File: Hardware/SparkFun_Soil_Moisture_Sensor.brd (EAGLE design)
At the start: 22.9 x 61 mm, 23 parts, among them J1 GATORGATOR_MINI, J2 GATORGATOR_MINI, J3 GATORGATOR_MINI, Q1 2N3904

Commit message: updating silk, fiducials
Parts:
- moved FID1 5.21 mm to (21.6, 56.1)
- moved FID4 5.21 mm to (21.6, 56.1)
- moved U$4 1.27 mm to (14.7, 55.0)
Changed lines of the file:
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@@
 <element name="LOGO1" library="SparkFun-Aesthetics" package="SFE_LOGO_NAME_FLAME_.1" value="SFE_LOGO_NAME_FLAME.1_INCH" x="17.399" y="45.847" smashed="yes" rot="MR0"/>
 <element name="LOGO2" library="SparkFun-Aesthetics" package="OSHW-LOGO-S" value="OSHW-LOGOS" x="20.32" y="54.61" smashed="yes" rot="MR0"/>
-<element name="U$4" library="SparkFun-Aesthetics" package="SFE_LOGO_FLAME_.2" value="" x="14.732" y="53.721" smashed="yes"/>
+<element name="U$4" library="SparkFun-Aesthetics" package="SFE_LOGO_FLAME_.2" value="" x="14.732" y="54.991" smashed="yes"/>
 <element name="STANDOFF1" library="SparkFun-Electromechanical" package="STAND-OFF" value="STAND-OFF" x="2.54" y="58.42" smashed="yes"/>
 <element name="STANDOFF2" library="SparkFun-Electromechanical" package="STAND-OFF" value="STAND-OFF" x="20.32" y="58.42" smashed="yes"/>
-<element name="FID1" library="SparkFun-Aesthetics" package="FIDUCIAL-1X2" value="FIDUCIAL1X2" x="17.78" y="59.69" smashed="yes"/>
+<element name="FID1" library="SparkFun-Aesthetics" package="FIDUCIAL-1X2" value="FIDUCIAL1X2" x="21.59" y="56.134" smashed="yes"/>
 <element name="FID2" library="SparkFun-Aesthetics" package="FIDUCIAL-1X2" value="FIDUCIAL1X2" x="1.27" y="45.72" smashed="yes"/>
 <element name="J1" library="SparkFun-Connectors" package="GATOR_MINI" value="GATORGATOR_MINI" x="3.81" y="52.07" smashed="yes" rot="R270"/>
@@
 <element name="J3" library="SparkFun-Connectors" package="GATOR_MINI" value="GATORGATOR_MINI" x="11.43" y="57.15" smashed="yes" rot="R180"/>
 <element name="FID3" library="SparkFun-Aesthetics" package="FIDUCIAL-1X2" value="FIDUCIAL1X2" x="1.27" y="45.72" smashed="yes" rot="MR0"/>
-<element name="FID4" library="SparkFun-Aesthetics" package="FIDUCIAL-1X2" value="FIDUCIAL1X2" x="17.78" y="59.69" smashed="yes" rot="MR0"/>
+<element name="FID4" library="SparkFun-Aesthetics" package="FIDUCIAL-1X2" value="FIDUCIAL1X2" x="21.59" y="56.134" smashed="yes" rot="MR0"/>
 <element name="U$1" library="buzzard_labels (2)" package="PWR2" value="" x="7.747" y="49.53" smashed="yes" rot="R90"/>
 <element name="U$2" library="buzzard_labels (2)" package="GND0" value="" x="15.24" y="54.483" smashed="yes" rot="R270"/>

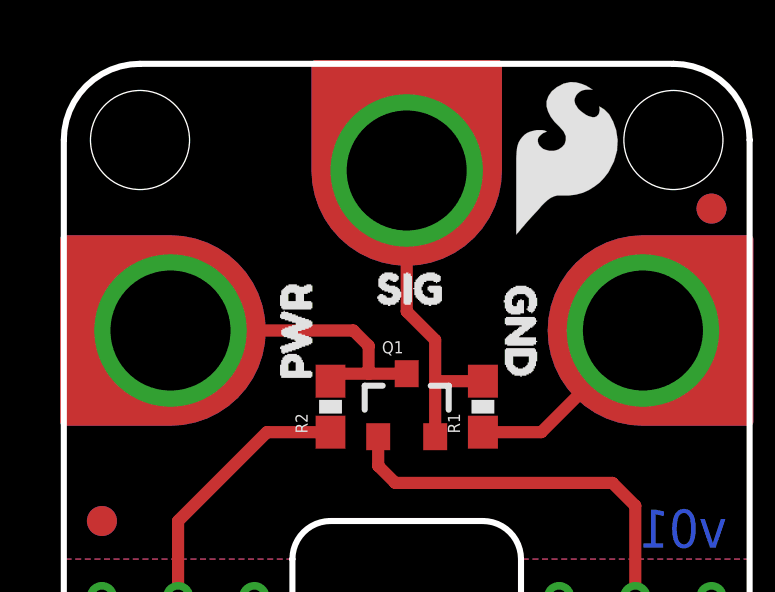
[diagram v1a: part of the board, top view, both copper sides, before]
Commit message: adding protection circuitry
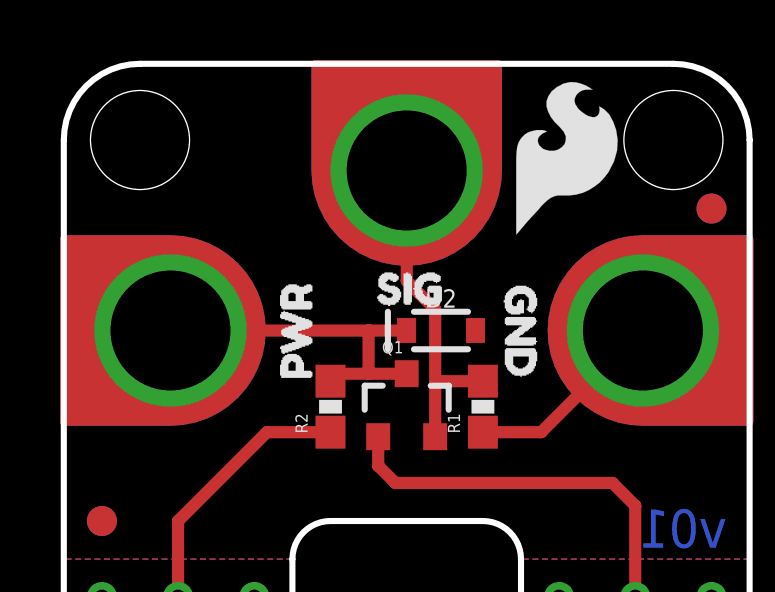
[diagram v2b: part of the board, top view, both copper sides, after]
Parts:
- added D2: 3.6V, SparkFun-DiscreteSemi:SOD-323
- Q1: device SparkFun-DiscreteSemi:SOT23-3 -> SparkFun-DiscreteSemi:SOT23-3@1
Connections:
- net GND: now also D2.A
- net VCC: now also D2.C
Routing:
- net VCC: track 10.4 -> 12.0 mm
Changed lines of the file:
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@@
 </autorouter>
 <elements>
-<element name="Q1" library="SparkFun-DiscreteSemi" package="SOT23-3" value="2N3904" x="11.43" y="49.53" smashed="yes">
+<element name="Q1" library="SparkFun-DiscreteSemi" package="SOT23-3@1" value="2N3904" x="11.43" y="49.53" smashed="yes">
 <attribute name="NAME" x="10.6045" y="51.308" size="0.4064" layer="25"/>
 <attribute name="PROD_ID" value="TRANS-08049" x="11.43" y="49.53" size="1.778" layer="27" font="vector" ratio="15" display="off"/>
@@
 <element name="U$7" library="buzzard_labels (2)" package="GND0" value="" x="15.24" y="49.657" smashed="yes" rot="MR90"/>
 <element name="LOGO3" library="SparkFun-Aesthetics" package="REVISION" value="REVISION" x="3.81" y="-12.7" smashed="yes"/>
+<element name="D2" library="SparkFun-DiscreteSemi" package="SOD-323" value="3.6V" x="12.573" y="52.07" smashed="yes">
+<attribute name="NAME" x="12.573" y="52.832" size="0.6096" layer="25" font="vector" ratio="20" align="bottom-center"/>
+<attribute name="PROD_ID" value="DIO-08199" x="12.573" y="52.07" size="1.778" layer="27" display="off"/>
+<attribute name="VALUE" x="12.573" y="51.308" size="0.6096" layer="27" font="vector" ratio="20" align="top-center"/>
+</element>
 </elements>
 <signals>
@@
 <contactref element="R1" pad="2"/>
 <contactref element="J3" pad="P$2"/>
-<wire x1="11.43" y1="57.404" x2="11.43" y2="52.705" width="0.4064" layer="1"/>
-<wire x1="11.43" y1="52.705" x2="12.38" y2="51.755" width="0.4064" layer="1"/>
-<wire x1="12.38" y1="51.755" x2="12.38" y2="50.292" width="0.4064" layer="1"/>
+<wire x1="11.43" y1="57.404" x2="11.43" y2="53.721" width="0.4064" layer="1"/>
+<wire x1="11.43" y1="53.721" x2="12.38" y2="52.771" width="0.4064" layer="1"/>
+<wire x1="12.38" y1="52.771" x2="12.38" y2="50.292" width="0.4064" layer="1"/>
 <wire x1="12.38" y1="50.292" x2="12.38" y2="48.53" width="0.4064" layer="1"/>
 <wire x1="12.468" y1="50.38" x2="12.38" y2="50.292" width="0.4064" layer="1"/>
@@
 <contactref element="J1" pad="P$2"/>
 <wire x1="10.16" y1="50.63" x2="11.43" y2="50.63" width="0.4064" layer="1"/>
-<wire x1="3.556" y1="52.07" x2="9.652" y2="52.07" width="0.4064" layer="1"/>
-<wire x1="9.652" y1="52.07" x2="10.16" y2="51.562" width="0.4064" layer="1"/>
-<wire x1="10.16" y1="51.562" x2="10.16" y2="50.63" width="0.4064" layer="1"/>
+<contactref element="D2" pad="C"/>
+<wire x1="3.556" y1="52.07" x2="10.16" y2="52.07" width="0.4064" layer="1"/>
+<wire x1="10.16" y1="52.07" x2="11.423" y2="52.07" width="0.4064" layer="1"/>
+<wire x1="10.16" y1="50.63" x2="10.16" y2="52.07" width="0.4064" layer="1"/>
 </signal>
 <signal name="GND">
@@
 <wire x1="19.304" y1="52.07" x2="15.914" y2="48.68" width="0.4064" layer="1"/>
 <wire x1="15.914" y1="48.68" x2="13.97" y2="48.68" width="0.4064" layer="1"/>
+<contactref element="D2" pad="A"/>
+<wire x1="13.723" y1="52.07" x2="13.97" y2="48.68" width="0" layer="19" extent="1-1"/>
 </signal>
 <signal name="PROBE1">

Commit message: finalizing silk and schematic before design review
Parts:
- added U$8: (no value), buzzard_labels (4):GATOR#SOIL_MOISTURE_SENSOR4
- added U$9: (no value), GatorBit_Final_for_Silk#01#png (2):GATORBIT_FINAL_FOR_SILK#01#PNG
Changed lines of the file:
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@@
 <?xml version="1.0" encoding="utf-8"?>
 <!DOCTYPE eagle SYSTEM "eagle.dtd">
-<eagle version="9.3.1">
+<eagle version="9.1.0">
 <drawing>
 <settings>
@@
 <attribute name="VALUE" x="12.573" y="51.308" size="0.6096" layer="27" font="vector" ratio="20" align="top-center"/>
 </element>
+<element name="U$8" library="buzzard_labels (4)" package="GATOR#SOIL_MOISTURE_SENSOR4" value="" x="1.524" y="46.99"/>
+<element name="U$9" library="GatorBit_Final_for_Silk#01#png (2)" package="GATORBIT_FINAL_FOR_SILK#01#PNG" value="" x="6.096" y="56.642"/>
 </elements>
 <signals>
@@
 <wire x1="15.914" y1="48.68" x2="13.97" y2="48.68" width="0.4064" layer="1"/>
 <contactref element="D2" pad="A"/>
-<wire x1="13.723" y1="52.07" x2="13.97" y2="48.68" width="0" layer="19" extent="1-1"/>
+<wire x1="13.97" y1="48.68" x2="13.723" y2="52.07" width="0" layer="19" extent="1-1"/>
 </signal>
 <signal name="PROBE1">

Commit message: engineer run of checklist
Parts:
- added U$10: (no value), SparkFun-Aesthetics:ORDERING_INSTRUCTIONS
- R1, R2: device SparkFun-Resistors:0603-RES -> SparkFun-Resistors:0603
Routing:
- net GND: track 6.74 -> 11.3 mm
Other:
- board text added: "Black Gloss Soldermask"
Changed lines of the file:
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@@
 <layer number="45" name="Holes" color="7" fill="1" visible="yes" active="yes"/>
 <layer number="46" name="Milling" color="3" fill="1" visible="no" active="yes"/>
-<layer number="47" name="Measures" color="7" fill="1" visible="no" active="yes"/>
+<layer number="47" name="Measures" color="7" fill="1" visible="yes" active="yes"/>
 <layer number="48" name="Document" color="7" fill="1" visible="no" active="yes"/>
 <layer number="49" name="Reference" color="7" fill="1" visible="no" active="yes"/>
@@
 <wire x1="20.32" y1="60.96" x2="22.86" y2="58.42" width="0.2032" layer="20" curve="-90"/>
 <text x="21.59" y="-12.7" size="1.778" layer="51" font="vector">Andy England</text>
+<text x="-5.08" y="-27.94" size="1.778" layer="51" font="vector">Black Gloss Soldermask</text>
 </plain>
 <attributes>
@@
 </class>
 </classes>
-<designrules name="SparkFun-2-layer">
-<description language="en">&lt;b&gt;EAGLE Design Rules&lt;/b&gt;
+<designrules name="SparkFun-2-layer-TIGHT">
+<description language="en">&lt;b&gt;SparkFun 2 Layer Design Rule Checks - STANDARD/TIGHT/FAB-LIMIT&lt;/b&gt;
 &lt;p&gt;
-The default Design Rules have been set to cover
-a wide range of applications. Your particular design
-may have different requirements, so please make the
-necessary adjustments and save your customized
-design rules under a new name.</description>
+These rules have been curated by SparkFuns DFM commitee. After doing much research, communicating with our multiple fab houses, and getting quotes of various designs, we have compiled three DRU files.
+&lt;p&gt;
+&lt;b&gt;STANDARD:&lt;/b&gt; This is more of a &quot;best case scenario&quot; set of limitations. If your design has the space, and/or you have the time to work within these parameters, please do. Larger trace width and clearance makes for easier visual inspection of the PCB while troubleshooting (useful in production and to the end user). It also allows for better ability to hack a trace (if you are crazy enough to scrape away the mask and solder to a trace). Another thing to keep in mind is that more metal is just more robust.
+&lt;p&gt;
+&lt;b&gt;TIGHT:&lt;/b&gt; This is where cost comes into play. We have found that most fab houses begin to add extra charges when you go smaller than these specs. In some cases, going to less than 15 mil trace can increase the cost by 10%. (This is why we have set the min drill on this DRU to 15 mil) Same story for traces thinner than 7 mil. To avoid those extra charges, then stay within the rules of this DRU.
+&lt;p&gt;
+&lt;b&gt;FAB-LIMIT:&lt;/b&gt; These set of rules are at the very limit of most fab houses capabilities. You will pay more for these specs, and it should be used on designs that have a darned good reason to need 4 mil vias and 4 mil traces.
+&lt;p&gt;
+**NOTE Clearance, Distance, Sizes, and Restring are all set to different limits in each of these three DRU files. Please compare the files within the CAM job editor window of eagle to see all the numbers.
+&lt;p&gt;
+***NOTE, Please set your Net Classes to default (0mil for all settings), so that it won't effect the DRC when you run it with these settings.</description>
 <param name="layerSetup" value="(1*16)"/>
 <param name="mtCopper" value="0.035mm 0.035mm 0.035mm 0.035mm 0.035mm 0.035mm 0.035mm 0.035mm 0.035mm 0.035mm 0.035mm 0.035mm 0.035mm 0.035mm 0.035mm 0.035mm"/>
 <param name="mtIsolate" value="1.5mm 0.15mm 0.2mm 0.15mm 0.2mm 0.15mm 0.2mm 0.15mm 0.2mm 0.15mm 0.2mm 0.15mm 0.2mm 0.15mm 0.2mm"/>
-<param name="mdWireWire" value="8mil"/>
-<param name="mdWirePad" value="8mil"/>
-<param name="mdWireVia" value="8mil"/>
-<param name="mdPadPad" value="8mil"/>
-<param name="mdPadVia" value="8mil"/>
-<param name="mdViaVia" value="8mil"/>
-<param name="mdSmdPad" value="8mil"/>
-<param name="mdSmdVia" value="8mil"/>
-<param name="mdSmdSmd" value="8mil"/>
+<param name="mdWireWire" value="7mil"/>
+<param name="mdWirePad" value="7mil"/>
+<param name="mdWireVia" value="7mil"/>
+<param name="mdPadPad" value="7mil"/>
+<param name="mdPadVia" value="7mil"/>
+<param name="mdViaVia" value="7mil"/>
+<param name="mdSmdPad" value="7mil"/>
+<param name="mdSmdVia" value="7mil"/>
+<param name="mdSmdSmd" value="7mil"/>
 <param name="mdViaViaSameLayer" value="8mil"/>
 <param name="mnLayersViaInSmd" value="2"/>
-<param name="mdCopperDimension" value="8mil"/>
-<param name="mdDrill" value="8mil"/>
+<param name="mdCopperDimension" value="7mil"/>
+<param name="mdDrill" value="7mil"/>
 <param name="mdSmdStop" value="0mil"/>
 <param name="msWidth" value="7mil"/>
@@
 <param name="rvMicroViaOuter" value="0.25"/>
 <param name="rvMicroViaInner" value="0.25"/>
-<param name="rlMinPadTop" value="12mil"/>
+<param name="rlMinPadTop" value="7mil"/>
 <param name="rlMaxPadTop" value="20mil"/>
-<param name="rlMinPadInner" value="10mil"/>
+<param name="rlMinPadInner" value="7mil"/>
 <param name="rlMaxPadInner" value="20mil"/>
-<param name="rlMinPadBottom" value="12mil"/>
+<param name="rlMinPadBottom" value="7mil"/>
 <param name="rlMaxPadBottom" value="20mil"/>
-<param name="rlMinViaOuter" value="10mil"/>
+<param name="rlMinViaOuter" value="7mil"/>
 <param name="rlMaxViaOuter" value="20mil"/>
-<param name="rlMinViaInner" value="10mil"/>
+<param name="rlMinViaInner" value="7mil"/>
 <param name="rlMaxViaInner" value="20mil"/>
 <param name="rlMinMicroViaOuter" value="4mil"/>
@@
 <param name="mlMinCreamFrame" value="0mil"/>
 <param name="mlMaxCreamFrame" value="0mil"/>
-<param name="mlViaStopLimit" value="20mil"/>
+<param name="mlViaStopLimit" value="25mil"/>
 <param name="srRoundness" value="0"/>
 <param name="srMinRoundness" value="0mil"/>
@@
 <attribute name="VALUE" x="10.414" y="49.3395" size="0.4064" layer="27"/>
 </element>
-<element name="R1" library="SparkFun-Resistors" package="0603-RES" value="10k" x="13.97" y="49.53" smashed="yes" rot="R90">
+<element name="R1" library="SparkFun-Resistors" package="0603" value="10k" x="13.97" y="49.53" smashed="yes" rot="R90">
 <attribute name="NAME" x="13.208" y="48.641" size="0.4064" layer="25" font="vector" rot="R90"/>
-<attribute name="PROD_ID" value="RES-12438" x="13.97" y="49.53" size="1.778" layer="27" font="vector" ratio="15" rot="R90" display="off"/>
-<attribute name="VALUE" x="15.113" y="48.514" size="0.4064" layer="27" font="vector" rot="R90"/>
+<attribute name="PROD_ID" value="RES-00824" x="13.97" y="49.53" size="1.778" layer="27" font="vector" ratio="15" rot="R90" display="off"/>
+<attribute name="VALUE" value="10k" x="15.113" y="48.514" size="0.4064" layer="27" font="vector" rot="R90"/>
 </element>
-<element name="R2" library="SparkFun-Resistors" package="0603-RES" value="100" x="8.89" y="49.53" smashed="yes" rot="R90">
+<element name="R2" library="SparkFun-Resistors" package="0603" value="100" x="8.89" y="49.53" smashed="yes" rot="R90">
 <attribute name="NAME" x="8.128" y="48.641" size="0.4064" layer="25" font="vector" rot="R90"/>
 <attribute name="PROD_ID" value="RES-12438" x="8.89" y="49.53" size="1.778" layer="27" font="vector" ratio="15" rot="R90" display="off"/>
-<attribute name="VALUE" x="10.033" y="48.514" size="0.4064" layer="27" font="vector" rot="R90"/>
+<attribute name="VALUE" value="100" x="10.033" y="48.514" size="0.4064" layer="27" font="vector" rot="R90"/>
 </element>
 <element name="FRAME1" library="SparkFun-Aesthetics" package="CREATIVE_COMMONS" value="" x="-7.62" y="-10.16" smashed="yes">
@@
 <element name="U$8" library="buzzard_labels (4)" package="GATOR#SOIL_MOISTURE_SENSOR4" value="" x="1.524" y="46.99"/>
 <element name="U$9" library="GatorBit_Final_for_Silk#01#png (2)" package="GATORBIT_FINAL_FOR_SILK#01#PNG" value="" x="6.096" y="56.642"/>
+<element name="U$10" library="SparkFun-Aesthetics" package="ORDERING_INSTRUCTIONS" value="" x="-6.35" y="-16.51"/>
 </elements>
 <signals>
@@
 <contactref element="J2" pad="P$2"/>
 <wire x1="19.304" y1="52.07" x2="15.914" y2="48.68" width="0.4064" layer="1"/>
-<wire x1="15.914" y1="48.68" x2="13.97" y2="48.68" width="0.4064" layer="1"/>
+<wire x1="15.914" y1="48.68" x2="15.24" y2="48.68" width="0.4064" layer="1"/>
 <contactref element="D2" pad="A"/>
-<wire x1="13.97" y1="48.68" x2="13.723" y2="52.07" width="0" layer="19" extent="1-1"/>
+<wire x1="15.24" y1="48.68" x2="13.97" y2="48.68" width="0.4064" layer="1"/>
+<wire x1="15.24" y1="48.68" x2="15.24" y2="51.435" width="0.4064" layer="1"/>
+<wire x1="15.24" y1="51.435" x2="14.605" y2="52.07" width="0.4064" layer="1"/>
+<wire x1="14.605" y1="52.07" x2="13.723" y2="52.07" width="0.4064" layer="1"/>
 </signal>
 <signal name="PROBE1">
@@
 <mfgpreviewcolor name="substratecolor" color="0xFF786E46"/>
 </mfgpreviewcolors>
+<errors>
+</errors>
 </board>
 </drawing>

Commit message: post qc double check, ordering protos
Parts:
- moved LOGO2 8.28 mm to (21.0, 46.4)
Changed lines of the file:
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@@
 </element>
 <element name="LOGO1" library="SparkFun-Aesthetics" package="SFE_LOGO_NAME_FLAME_.1" value="SFE_LOGO_NAME_FLAME.1_INCH" x="17.399" y="45.847" smashed="yes" rot="MR0"/>
-<element name="LOGO2" library="SparkFun-Aesthetics" package="OSHW-LOGO-S" value="OSHW-LOGOS" x="20.32" y="54.61" smashed="yes" rot="MR0"/>
+<element name="LOGO2" library="SparkFun-Aesthetics" package="OSHW-LOGO-S" value="OSHW-LOGOS" x="20.955" y="46.355" smashed="yes" rot="MR0"/>
 <element name="U$4" library="SparkFun-Aesthetics" package="SFE_LOGO_FLAME_.2" value="" x="14.732" y="54.991" smashed="yes"/>
 <element name="STANDOFF1" library="SparkFun-Electromechanical" package="STAND-OFF" value="STAND-OFF" x="2.54" y="58.42" smashed="yes"/>

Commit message: engineer run of checklist
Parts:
- removed U$9: (no value), GatorBit_Final_for_Silk#01#png (2):GATORBIT_FINAL_FOR_SILK#01#PNG
- added U$11: (no value), GatorBit_Final_for_Silk#01#png (3):GATORBIT_FINAL_FOR_SILK#01#PNG
- U$8: device buzzard_labels (4):GATOR#SOIL_MOISTURE_SENSOR4 -> buzzard_labels (16):GATOR#SOIL1
- moved LOGO2 17.1 mm to (3.81, 46.1)
- moved U$8 4.83 mm to (6.35, 47.0)
- moved U$4 0.25 mm to (14.5, 55.0)
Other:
- board text added: "v10"
- board text removed: "v01"
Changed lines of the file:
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@@
 <vertex x="22.86" y="44.45"/>
 </polygon>
-<text x="22.098" y="44.831" size="1.27" layer="16" font="vector" ratio="15" rot="SMR0">v01</text>
+<text x="22.098" y="44.831" size="1.27" layer="16" font="vector" ratio="15" rot="SMR0">v10</text>
 <wire x1="2.54" y1="60.96" x2="20.32" y2="60.96" width="0.2032" layer="20"/>
 <wire x1="0" y1="58.42" x2="2.54" y2="60.96" width="0.2032" layer="20" curve="-90"/>
@@
 </element>
 <element name="LOGO1" library="SparkFun-Aesthetics" package="SFE_LOGO_NAME_FLAME_.1" value="SFE_LOGO_NAME_FLAME.1_INCH" x="17.399" y="45.847" smashed="yes" rot="MR0"/>
-<element name="LOGO2" library="SparkFun-Aesthetics" package="OSHW-LOGO-S" value="OSHW-LOGOS" x="20.955" y="46.355" smashed="yes" rot="MR0"/>
-<element name="U$4" library="SparkFun-Aesthetics" package="SFE_LOGO_FLAME_.2" value="" x="14.732" y="54.991" smashed="yes"/>
+<element name="LOGO2" library="SparkFun-Aesthetics" package="OSHW-LOGO-S" value="OSHW-LOGOS" x="3.81" y="46.101" smashed="yes" rot="MR0"/>
+<element name="U$4" library="SparkFun-Aesthetics" package="SFE_LOGO_FLAME_.2" value="" x="14.478" y="54.991" smashed="yes"/>
 <element name="STANDOFF1" library="SparkFun-Electromechanical" package="STAND-OFF" value="STAND-OFF" x="2.54" y="58.42" smashed="yes"/>
 <element name="STANDOFF2" library="SparkFun-Electromechanical" package="STAND-OFF" value="STAND-OFF" x="20.32" y="58.42" smashed="yes"/>
@@
 <attribute name="VALUE" x="12.573" y="51.308" size="0.6096" layer="27" font="vector" ratio="20" align="top-center"/>
 </element>
-<element name="U$8" library="buzzard_labels (4)" package="GATOR#SOIL_MOISTURE_SENSOR4" value="" x="1.524" y="46.99"/>
-<element name="U$9" library="GatorBit_Final_for_Silk#01#png (2)" package="GATORBIT_FINAL_FOR_SILK#01#PNG" value="" x="6.096" y="56.642"/>
 <element name="U$10" library="SparkFun-Aesthetics" package="ORDERING_INSTRUCTIONS" value="" x="-6.35" y="-16.51"/>
+<element name="U$11" library="GatorBit_Final_for_Silk#01#png (3)" package="GATORBIT_FINAL_FOR_SILK#01#PNG" value="" x="19.304" y="46.609"/>
+<element name="U$8" library="buzzard_labels (16)" package="GATOR#SOIL1" value="" x="6.35" y="46.99"/>
 </elements>
 <signals>
